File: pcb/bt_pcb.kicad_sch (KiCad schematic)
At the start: 1 part, among them IC4 STM32H750VBT6

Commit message: progress on audio pcb
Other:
- sheet Codec and audio IO ports: added 3V3, CTRL_MC/SCL/FMT, CTRL_MD/SCA/DEMP, CTRL_MS/ADR/IFMD, CTRL_RST, DEC_BCK, DEC_DIN, DEC_LRCK, DEC_SCK, ENC_BCK, ENC_DOUT, ENC_LRCK, ENC_SCK, GND, VCC, VOUTL, VOUTR; removed none
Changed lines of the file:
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@@
 (kicad_sch (version 20230121) (generator eeschema)
   (paper "A4")
+  (wire (pts (xy 71.882 67.564) (xy 89.027 67.564))
+    (stroke (width 0) (type default))
+  )
+  (wire (pts (xy 61.214 42.418) (xy 71.882 42.418))
+    (stroke (width 0) (type default))
+  )
+  (wire (pts (xy 71.882 42.418) (xy 71.882 67.564))
+    (stroke (width 0) (type default))
+  )
+  (wire (pts (xy 89.027 69.596) (xy 70.104 69.596))
+    (stroke (width 0) (type default))
+  )
+  (wire (pts (xy 70.104 71.628) (xy 70.104 77.47))
+    (stroke (width 0) (type default))
+  )
+  (wire (pts (xy 70.104 69.596) (xy 70.104 44.45))
+    (stroke (width 0) (type default))
+  )
+  (wire (pts (xy 61.214 44.45) (xy 70.104 44.45))
+    (stroke (width 0) (type default))
+  )
+  (wire (pts (xy 89.027 71.628) (xy 70.104 71.628))
+    (stroke (width 0) (type default))
+  )
+  (symbol (lib_id "power:GND") (at 70.104 77.47 0) (unit 1)
+    (in_bom yes) (on_board yes) (dnp no) (fields_autoplaced)
+    (property "Reference" "#PWR07" (at 70.104 83.82 0)
+      (effects (font (size 1.27 1.27)) hide)
+    )
+    (property "Value" "GND" (at 70.104 82.55 0)
+      (effects (font (size 1.27 1.27)))
+    )
+    (property "Footprint" "" (at 70.104 77.47 0)
+      (effects (font (size 1.27 1.27)) hide)
+    )
+    (property "Datasheet" "" (at 70.104 77.47 0)
+      (effects (font (size 1.27 1.27)) hide)
+    )
+    (pin "1")
+    (instances
+      (project "bt_pcb"
+        (path "/eb787481-08cd-41a4-a128-173fa6227c32"
+          (reference "#PWR07") (unit 1)
+        )
+      )
+    )
+  )
   (symbol (lib_id "SamacSys_Parts:STM32H750VBT6") (at 131.445 87.63 0) (unit 1)
     (in_bom yes) (on_board yes) (dnp no) (fields_autoplaced)
@@
     )
   )
-  (sheet (at 76.2 83.185) (size 27.305 23.495) (fields_autoplaced)
+  (sheet (at 89.027 65.532) (size 27.305 37.084) (fields_autoplaced)
     (stroke (width 0.1524) (type solid))
     (fill (color 0 0 0 0.0000))
-    (property "Sheetname" "Codec and audio IO" (at 76.2 82.4734 0)
+    (property "Sheetname" "Codec and audio IO" (at 89.027 64.8204 0)
       (effects (font (size 1.27 1.27)) (justify left bottom))
     )
-    (property "Sheetfile" "codec_and_audio.kicad_sch" (at 76.2 107.2646 0)
+    (property "Sheetfile" "codec_and_audio.kicad_sch" (at 89.027 103.2006 0)
       (effects (font (size 1.27 1.27)) (justify left top))
+    )
+    (pin "3V3" input (at 89.027 67.564 180)
+      (effects (font (size 1.27 1.27)) (justify left))
+    )
+    (pin "CTRL_MC{slash}SCL{slash}FMT" bidirectional (at 89.027 76.708 180)
+      (effects (font (size 1.27 1.27)) (justify left))
+    )
+    (pin "CTRL_MD{slash}SCA{slash}DEMP" bidirectional (at 89.027 78.74 180)
+      (effects (font (size 1.27 1.27)) (justify left))
+    )
+    (pin "ENC_LRCK" bidirectional (at 89.027 91.44 180)
+      (effects (font (size 1.27 1.27)) (justify left))
+    )
+    (pin "ENC_SCK" input (at 89.027 85.344 180)
+      (effects (font (size 1.27 1.27)) (justify left))
+    )
+    (pin "ENC_DOUT" output (at 89.027 89.408 180)
+      (effects (font (size 1.27 1.27)) (justify left))
+    )
+    (pin "ENC_BCK" bidirectional (at 89.027 87.376 180)
+      (effects (font (size 1.27 1.27)) (justify left))
+    )
+    (pin "GND" input (at 89.027 71.628 180)
+      (effects (font (size 1.27 1.27)) (justify left))
+    )
+    (pin "VCC" input (at 89.027 69.596 180)
+      (effects (font (size 1.27 1.27)) (justify left))
+    )
+    (pin "VOUTR" output (at 116.332 86.868 0)
+      (effects (font (size 1.27 1.27)) (justify right))
+    )
+    (pin "VOUTL" output (at 116.332 88.9 0)
+      (effects (font (size 1.27 1.27)) (justify right))
+    )
+    (pin "CTRL_RST" input (at 89.027 80.772 180)
+      (effects (font (size 1.27 1.27)) (justify left))
+    )
+    (pin "DEC_DIN" input (at 89.027 98.298 180)
+      (effects (font (size 1.27 1.27)) (justify left))
+    )
+    (pin "CTRL_MS{slash}ADR{slash}IFMD" bidirectional (at 89.027 74.676 180)
+      (effects (font (size 1.27 1.27)) (justify left))
+    )
+    (pin "DEC_LRCK" bidirectional (at 89.027 100.33 180)
+      (effects (font (size 1.27 1.27)) (justify left))
+    )
+    (pin "DEC_SCK" input (at 89.027 94.234 180)
+      (effects (font (size 1.27 1.27)) (justify left))
+    )
+    (pin "DEC_BCK" bidirectional (at 89.027 96.266 180)
+      (effects (font (size 1.27 1.27)) (justify left))
     )
     (instances
@@
     )
   )
-  (sheet (at 36.195 38.735) (size 27.94 8.89) (fields_autoplaced)
+  (sheet (at 34.671 40.005) (size 26.543 8.89) (fields_autoplaced)
     (stroke (width 0.1524) (type solid))
     (fill (color 0 0 0 0.0000))
-    (property "Sheetname" "Power Supply" (at 36.195 38.0234 0)
+    (property "Sheetname" "Power Supply" (at 34.671 39.2934 0)
       (effects (font (size 1.27 1.27)) (justify left bottom))
     )
-    (property "Sheetfile" "power_supply.kicad_sch" (at 36.195 48.2096 0)
+    (property "Sheetfile" "power_supply.kicad_sch" (at 34.671 49.4796 0)
       (effects (font (size 1.27 1.27)) (justify left top))
     )
-    (pin "3V3" output (at 64.135 41.275 0)
-      (effects (font (size 1.27 1.27)) (justify right))
-    )
-    (pin "5V" output (at 64.135 45.085 0)
-      (effects (font (size 1.27 1.27)) (justify right))
-    )
+    (pin "3V3" output (at 61.214 42.418 0)
+      (effects (font (size 1.27 1.27)) (justify right))
+    )
+    (pin "5V" output (at 61.214 44.45 0)
+      (effects (font (size 1.27 1.27)) (justify right))
+    )

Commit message: progress on understanding audio schematics
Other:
- sheet Codec and audio IO ports: added VDD; removed 3V3, GND, VOUTL, VOUTR
- moved on the sheet: IC4

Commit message: progress on shcematics
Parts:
- added C19, C20: 20p, symbol Device:C
- added C21, C22, C23, C24, C27, C28, C32, C34: 100n, symbol Device:C
- added C26: 1u, symbol Device:C
- added C29, C30: 2u2, symbol Device:C
- added D2: LED, symbol Device:LED
- added J2: Conn_JTAG_SWD_10, symbol Connector:Conn_ARM_JTAG_SWD_10
- added R3, R5: 10k, symbol Device:R
- added R4: 1k, symbol Device:R
- added Y1: Crystal, symbol Device:Crystal
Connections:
- net GND: now reaches IC4.10 (VSS_1)
- net GND: now also IC4.19 (VSSA), IC4.26 (VSS_2), IC4.49 (VSS_3), IC4.74 (VSS_4), IC4.99 (VSS_5), C19.1, C20.1, C21.1, C22.2, C23.2, C24.2, C26.2, C27.2, C28.2, C29.2, C30.2, C32.1, C34.1, D2.1 (K), J2.3 (GND), J2.5 (GND), J2.9 (GNDDetect), R3.1
- net 3V3: now reaches IC4.100 (VDD_5)
- net 3V3: now also IC4.11 (VDD_1), IC4.20 (VREF+), IC4.21 (VDDA), IC4.27 (VDD_2), IC4.50 (VDD_3), IC4.6 (VBAT), IC4.75 (VDD_4), C22.1, C23.1, C24.1, C26.1, C27.1, C28.1, C32.2, C34.2, J2.1 (VTref), R4.1, R5.1
- net at IC4.12 (PH0-OSC_IN): now also C19.2, Y1.2
- net at IC4.13 (PH1-OSC_OUT): now also C20.2, Y1.1
- net NRST: now reaches IC4.14 (NRST)
- net NRST: now also C21.2, J2.10 (~{RESET}), R5.2
- net I2S1_WS: now reaches IC4.28 (PA4)
- net I2S1_CK: now reaches IC4.29 (PA5)
- net I2S1_SDI: now reaches IC4.30 (PA6)
- net I2S1_SDO: now reaches IC4.31 (PA7)
- net I2S1_MCK: now reaches IC4.32 (PC4)
- net at IC4.48 (VCAP_1): now also C29.1
- net DEB_JTMS_SWDIO: now reaches IC4.72 (PA13)
- net DEB_JTMS_SWDIO: now also J2.2 (SWDIO/TMS)
- net at IC4.73 (VCAP_2): now also C30.1
- net DEB_JTCK_SWCLK: now reaches IC4.76 (PA14)
- net DEB_JTCK_SWCLK: now also J2.4 (SWCLK/TCK)
- net DEB_JTDI: now reaches IC4.77 (PA15)
- net DEB_JTDI: now also J2.8 (NC/TDI)
- net DEB_JTDO_SWO: now reaches IC4.89 (PB3)
- net DEB_JTDO_SWO: now also J2.6 (SWO/TDO)
- net at IC4.94 (BOOT0): now also R3.2
- new net: D2.2 (A), R4.2
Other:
- note added: "TODO LIST: - check the voltage references - finish the codec - make the sd card - and much more"
- note added: "for pcm3060 - LRCK word select - BCK bit clock - DIN line from ADC - DOUT line to DAC - SCK == 256 * FS (system operation)"
- note added: "for stm32h750 - WS word select 1xFS - CK bit clock resxFS - SDI input from ADC - SDO output to DAC - MCK 256xFS???"
- note added: "from wikipedia for i2s specs: - SCK == BCLK - WS == LRCLK or FS - SD == SDIN or SDOUT - MCK == 256xLRCLK"
- note added: "no need for the 32k osc"
- note added: "not sure about nrst"
- note added: "tms tclk tdo tdi nrst"
- note added: "vtref gnd gnd KEY gnd"
- moved on the sheet: IC4

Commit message: update
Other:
- note added: "TODO LIST: - finish the codec - make the sd card - 5v power input from usb - UI - display and leds - adc for externals - rotary encoders"
- note removed: "TODO LIST: - check the voltage references - finish the codec - make the sd card - and much more"
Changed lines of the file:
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@@
     (effects (font (size 1.27 1.27)) (justify left bottom))
   )
-  (text "TODO LIST:\n- check the voltage references\n- finish the codec\n- make the sd card\n- and much more"
-    (at 55.245 80.645 0)
+  (text "TODO LIST:\n- finish the codec\n- make the sd card\n- 5v power input from usb\n- UI\n  - display and leds\n  - adc for externals\n  - rotary encoders"
+    (at 31.75 95.885 0)
     (effects (font (size 2.54 2.54)) (justify left bottom))
   )

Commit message: aaaaaa
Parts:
- added J6: Micro_SD_Card, symbol Connector:Micro_SD_Card
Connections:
- net GND: now also J6.9 (SHIELD)
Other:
- sheet Codec and audio IO ports: added none; removed CTRL_MC/SCL/FMT, CTRL_MD/SCA/DEMP, CTRL_MS/ADR/IFMD, CTRL_RST, DEC_BCK, DEC_DIN, DEC_LRCK, DEC_SCK, ENC_BCK, ENC_DOUT, ENC_LRCK, ENC_SCK, VCC, VDD
- moved on the sheet: D2, R4

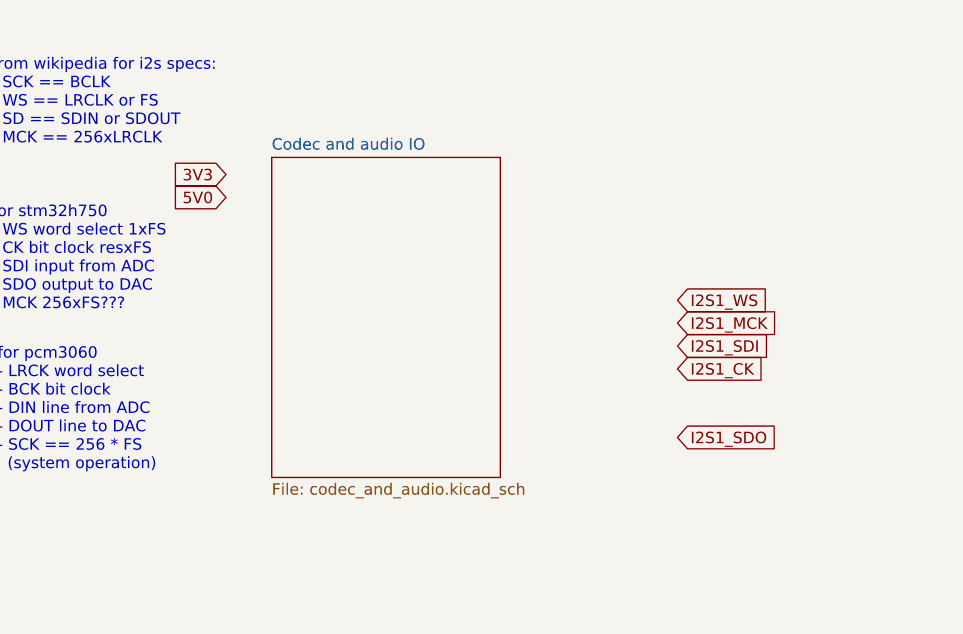
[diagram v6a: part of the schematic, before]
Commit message: some more pages for the schematic
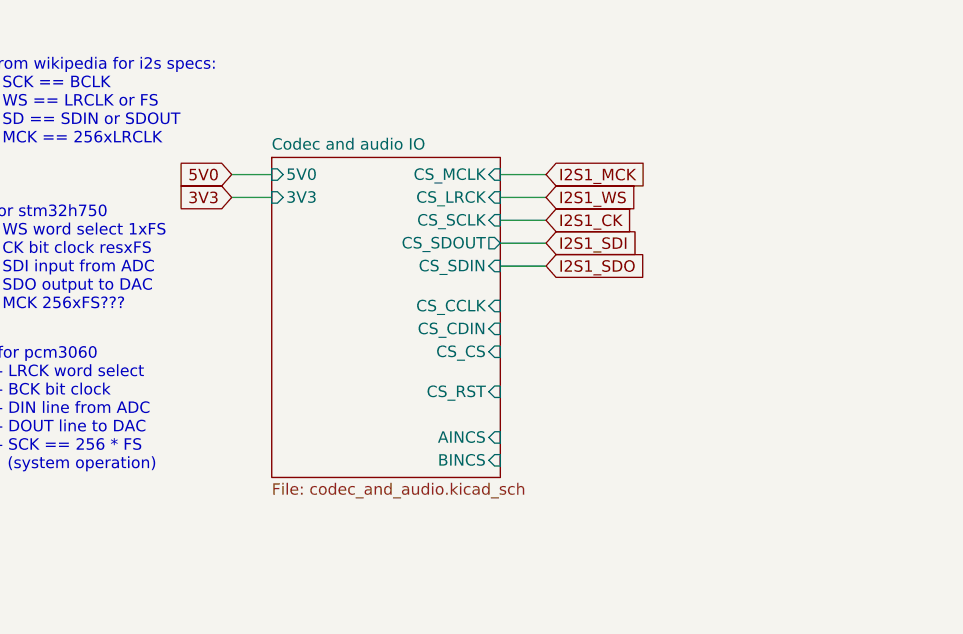
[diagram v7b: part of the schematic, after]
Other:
- sheet Codec and audio IO ports: added 3V3, 5V0, AINCS, BINCS, CS_CCLK, CS_CDIN, CS_CS, CS_LRCK, CS_MCLK, CS_RST, CS_SCLK, CS_SDIN, CS_SDOUT; removed none
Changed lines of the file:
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@@
+    (stroke (width 0) (type default))
+  )
+  (wire (pts (xy 72.39 158.75) (xy 77.47 158.75))
     (stroke (width 0) (type default))
   )
@@
     (stroke (width 0) (type default))
   )
+  (wire (pts (xy 72.39 166.37) (xy 77.47 166.37))
+    (stroke (width 0) (type default))
+  )
   (wire (pts (xy 179.705 100.965) (xy 247.65 100.965))
     (stroke (width 0) (type default))
@@
     (stroke (width 0) (type default))
   )
+  (wire (pts (xy 72.39 161.29) (xy 77.47 161.29))
+    (stroke (width 0) (type default))
+  )
   (wire (pts (xy 222.885 116.205) (xy 247.65 116.205))
     (stroke (width 0) (type default))
@@
     (stroke (width 0) (type default))
   )
+  (wire (pts (xy 42.545 158.75) (xy 46.99 158.75))
+    (stroke (width 0) (type default))
+  )
   (wire (pts (xy 204.47 103.505) (xy 247.65 103.505))
     (stroke (width 0) (type default))
   )
+  (wire (pts (xy 72.39 163.83) (xy 77.47 163.83))
+    (stroke (width 0) (type default))
+  )
   (wire (pts (xy 270.51 50.165) (xy 270.51 52.705))
     (stroke (width 0) (type default))
@@
   )
   (wire (pts (xy 168.91 100.965) (xy 170.815 100.965))
+    (stroke (width 0) (type default))
+  )
+  (wire (pts (xy 72.39 168.91) (xy 77.47 168.91))
+    (stroke (width 0) (type default))
+  )
+  (wire (pts (xy 42.545 161.29) (xy 46.99 161.29))
     (stroke (width 0) (type default))
   )
@@
     )
   )
-  (global_label "I2S1_MCK" (shape input) (at 92.075 175.26 0) (fields_autoplaced)
+  (global_label "I2S1_MCK" (shape input) (at 77.47 158.75 0) (fields_autoplaced)
     (effects (font (size 1.27 1.27)) (justify left))
-    (property "Intersheetrefs" "${INTERSHEET_REFS}" (at 104.2525 175.26 0)
+    (property "Intersheetrefs" "${INTERSHEET_REFS}" (at 89.6475 158.75 0)
       (effects (font (size 1.27 1.27)) (justify left) hide)
     )
@@
     )
   )
-  (global_label "I2S1_SDI" (shape input) (at 92.075 177.8 0) (fields_autoplaced)
+  (global_label "I2S1_SDI" (shape input) (at 77.47 166.37 0) (fields_autoplaced)
     (effects (font (size 1.27 1.27)) (justify left))
-    (property "Intersheetrefs" "${INTERSHEET_REFS}" (at 103.3454 177.8 0)
+    (property "Intersheetrefs" "${INTERSHEET_REFS}" (at 88.7404 166.37 0)
       (effects (font (size 1.27 1.27)) (justify left) hide)
     )
@@
     )
   )
-  (global_label "3V3" (shape input) (at 41.91 158.75 180) (fields_autoplaced)
-    (effects (font (size 1.27 1.27)) (justify right))
-    (property "Intersheetrefs" "${INTERSHEET_REFS}" (at 35.4172 158.75 0)
-      (effects (font (size 1.27 1.27)) (justify right) hide)
-    )
-  )
-  (global_label "I2S1_SDO" (shape input) (at 92.075 187.96 0) (fields_autoplaced)
+  (global_label "3V3" (shape input) (at 42.545 161.29 180) (fields_autoplaced)
+    (effects (font (size 1.27 1.27)) (justify right))
+    (property "Intersheetrefs" "${INTERSHEET_REFS}" (at 36.0522 161.29 0)
+      (effects (font (size 1.27 1.27)) (justify right) hide)
+    )
+  )
+  (global_label "I2S1_SDO" (shape input) (at 77.47 168.91 0) (fields_autoplaced)
     (effects (font (size 1.27 1.27)) (justify left))
-    (property "Intersheetrefs" "${INTERSHEET_REFS}" (at 104.0711 187.96 0)
+    (property "Intersheetrefs" "${INTERSHEET_REFS}" (at 89.4661 168.91 0)
       (effects (font (size 1.27 1.27)) (justify left) hide)
     )
   )
-  (global_label "I2S1_WS" (shape input) (at 92.075 172.72 0) (fields_autoplaced)
+  (global_label "I2S1_WS" (shape input) (at 77.47 161.29 0) (fields_autoplaced)
     (effects (font (size 1.27 1.27)) (justify left))
-    (property "Intersheetrefs" "${INTERSHEET_REFS}" (at 102.922 172.72 0)
+    (property "Intersheetrefs" "${INTERSHEET_REFS}" (at 88.317 161.29 0)
       (effects (font (size 1.27 1.27)) (justify left) hide)
     )
@@
     )
   )
-  (global_label "5V0" (shape input) (at 41.91 161.29 180) (fields_autoplaced)
-    (effects (font (size 1.27 1.27)) (justify right))
-    (property "Intersheetrefs" "${INTERSHEET_REFS}" (at 35.4172 161.29 0)
+  (global_label "5V0" (shape input) (at 42.545 158.75 180) (fields_autoplaced)
+    (effects (font (size 1.27 1.27)) (justify right))
+    (property "Intersheetrefs" "${INTERSHEET_REFS}" (at 36.0522 158.75 0)
       (effects (font (size 1.27 1.27)) (justify right) hide)
     )
@@
     )
   )
-  (global_label "I2S1_CK" (shape input) (at 92.075 180.34 0) (fields_autoplaced)
+  (global_label "I2S1_CK" (shape input) (at 77.47 163.83 0) (fields_autoplaced)
     (effects (font (size 1.27 1.27)) (justify left))
-    (property "Intersheetrefs" "${INTERSHEET_REFS}" (at 102.8011 180.34 0)
+    (property "Intersheetrefs" "${INTERSHEET_REFS}" (at 88.1961 163.83 0)
       (effects (font (size 1.27 1.27)) (justify left) hide)
     )
@@
       (effects (font (size 1.27 1.27)) (justify left top))
     )
-    (instances
+    (pin "CS_CS" input (at 72.39 178.435 0)
+      (effects (font (size 1.27 1.27)) (justify right))
+    )
+    (pin "CS_CDIN" input (at 72.39 175.895 0)
+      (effects (font (size 1.27 1.27)) (justify right))
+    )
+    (pin "CS_RST" input (at 72.39 182.88 0)
+      (effects (font (size 1.27 1.27)) (justify right))
+    )
+    (pin "CS_SDIN" input (at 72.39 168.91 0)
+      (effects (font (size 1.27 1.27)) (justify right))
+    )
+    (pin "CS_LRCK" input (at 72.39 161.29 0)
+      (effects (font (size 1.27 1.27)) (justify right))
+    )
+    (pin "CS_CCLK" input (at 72.39 173.355 0)
+      (effects (font (size 1.27 1.27)) (justify right))
+    )
+    (pin "CS_MCLK" input (at 72.39 158.75 0)
+      (effects (font (size 1.27 1.27)) (justify right))
+    )
+    (pin "CS_SDOUT" output (at 72.39 166.37 0)
+      (effects (font (size 1.27 1.27)) (justify right))
+    )
+    (pin "CS_SCLK" input (at 72.39 163.83 0)
+      (effects (font (size 1.27 1.27)) (justify right))
+    )
+    (pin "5V0" input (at 46.99 158.75 180)
+      (effects (font (size 1.27 1.27)) (justify left))
+    )
+    (pin "3V3" input (at 46.99 161.29 180)
+      (effects (font (size 1.27 1.27)) (justify left))
+    )
+    (pin "BINCS" input (at 72.39 190.5 0)
+      (effects (font (size 1.27 1.27)) (justify right))
+    )
+    (pin "AINCS" input (at 72.39 187.96 0)
+      (effects (font (size 1.27 1.27)) (justify right))
+    )
+    (instances

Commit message: big progress!
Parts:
- added C68: 2u2, symbol Device:C
- added IC5: W25Q512JVEIM, SON127P800X600X80-9N-D, symbol SamacSys_Parts:W25Q512JVEIM
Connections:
- net 3V3 is gone; now on net +3V3: C22.1, C23.1, C24.1, C26.1, C27.1, C28.1, C32.2, C34.2, IC4.100 (VDD_5), IC4.11 (VDD_1), IC4.20 (VREF+), IC4.21 (VDDA), IC4.27 (VDD_2), IC4.50 (VDD_3), IC4.6 (VBAT), IC4.75 (VDD_4), J2.1 (VTref), R4.1, R5.1
- net GND: now also J6.6 (VSS), C68.2, IC5.4 (GND), IC5.9 (EP)
- net +3V3: now reaches J6.4 (VDD)
- net +3V3: now also C68.1, IC5.3 (~{WP_(IO2)}), IC5.7 (~{HOLD_OR_}/RESET_(IO3)), IC5.8 (VCC)
- net CODEC_RST: now reaches IC4.45 (PE15)
- net CODEC_I2C_SCL: now reaches IC4.46 (PB10)
- net CODEC_I2C_SDA: now reaches IC4.47 (PB11)
- net F_SPI_CS: now reaches IC4.51 (PB12)
- net F_SPI_CS: now also IC5.1 (~{CS})
- net F_SPI_CLK: now reaches IC4.52 (PB13)
- net F_SPI_CLK: now also IC5.6 (CLK)
- net F_SPI_MISO: now reaches IC4.53 (PB14)
- net F_SPI_MISO: now also IC5.2 (DO_(IO1))
- net F_SPI_MOSI: now reaches IC4.54 (PB15)
- net F_SPI_MOSI: now also IC5.5 (DI_(IO0))
- net I2S1_CK renamed CODEC_I2S_CK
- net I2S1_MCK renamed CODEC_I2S_MCK
- net I2S1_SDI renamed CODEC_I2S_SDI
- net I2S1_SDO renamed CODEC_I2S_SDO
- net I2S1_WS renamed CODEC_I2S_WS
- no-connect marks 0 -> 2
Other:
- sheet Codec and audio IO ports: added CS_SCL, CS_SDA; removed CS_CCLK, CS_CDIN, CS_CS
- sheet Power Supply ports: added 5V0; removed 5V
- note added: "TODO LIST: - make the sd card - UI - display and leds - adc for externals - rotary encoders"
- note removed: "TODO LIST: - finish the codec - make the sd card - 5v power input from usb - UI - display and leds - adc for externals - rotary encoders"
- note removed: "no need for the 32k osc"
- moved on the sheet: C22, C23, C24, C26, C27, C28, C29, C34, J2, R3
